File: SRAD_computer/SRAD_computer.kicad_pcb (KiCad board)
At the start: 2 copper layers, 49 parts, among them J1 USB_B_Micro, J2 Conn_01x02, U1 NCP1117-3.3_SOT223, U2 W25Q128JVS, U3 RP2040, U4 BME280, U5 MPU-9250, U6 SAM-M8Q-0-10, Y1 ABM8-272-T3

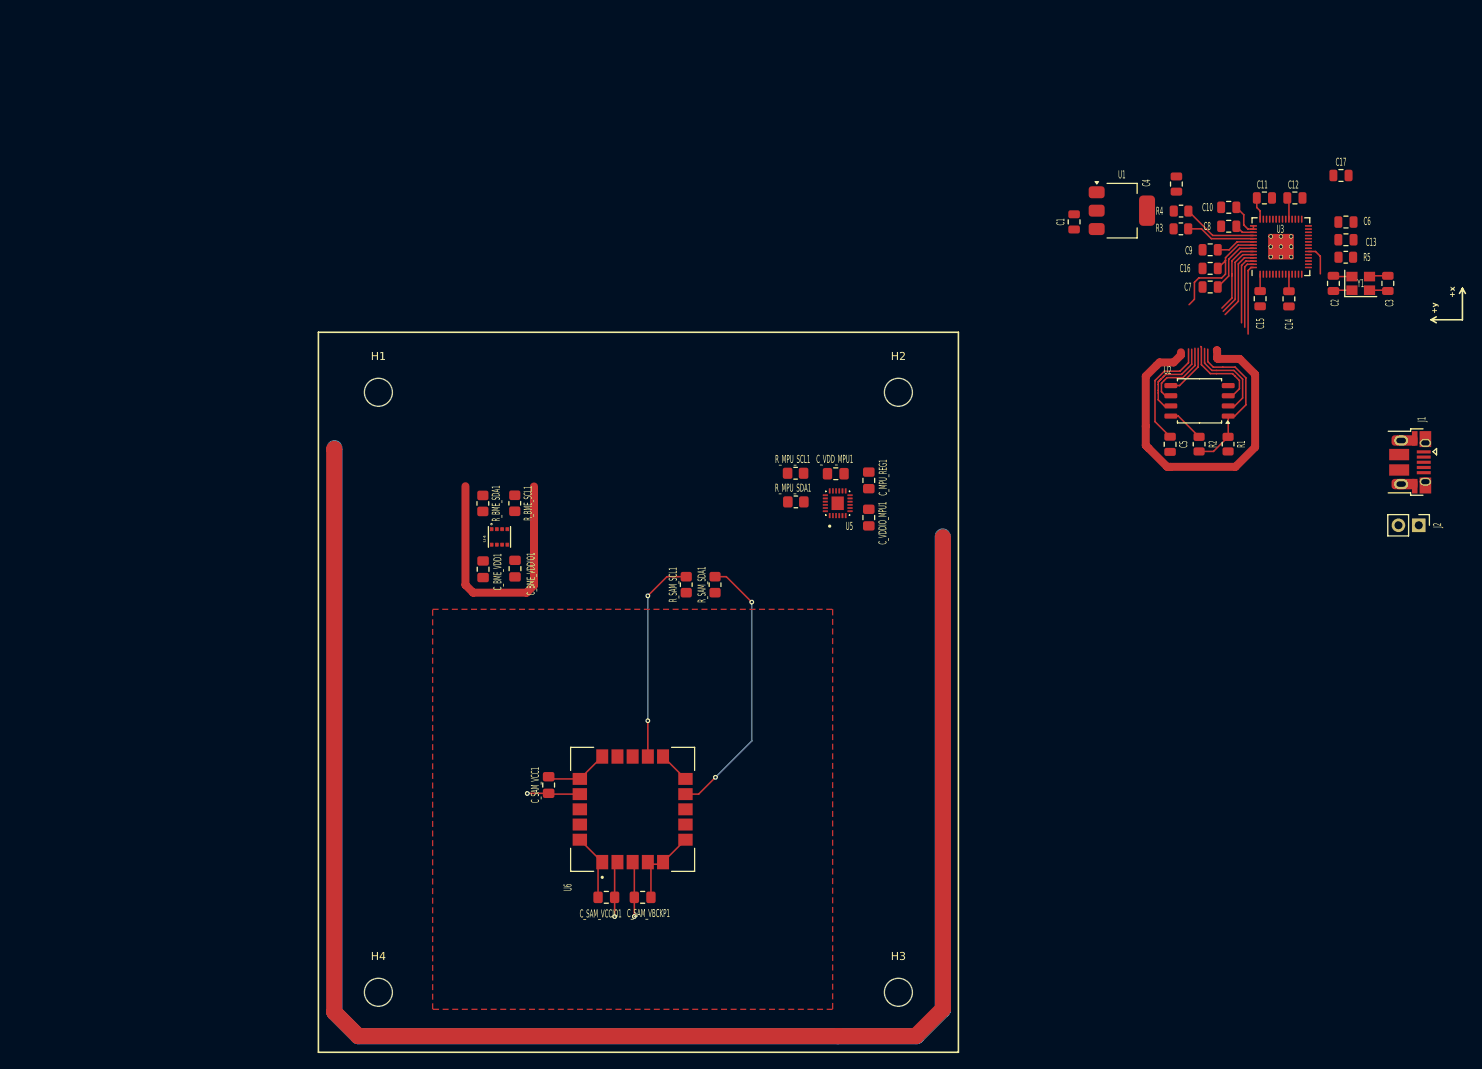
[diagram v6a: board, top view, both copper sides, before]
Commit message: Update PCB placement & 3D models added
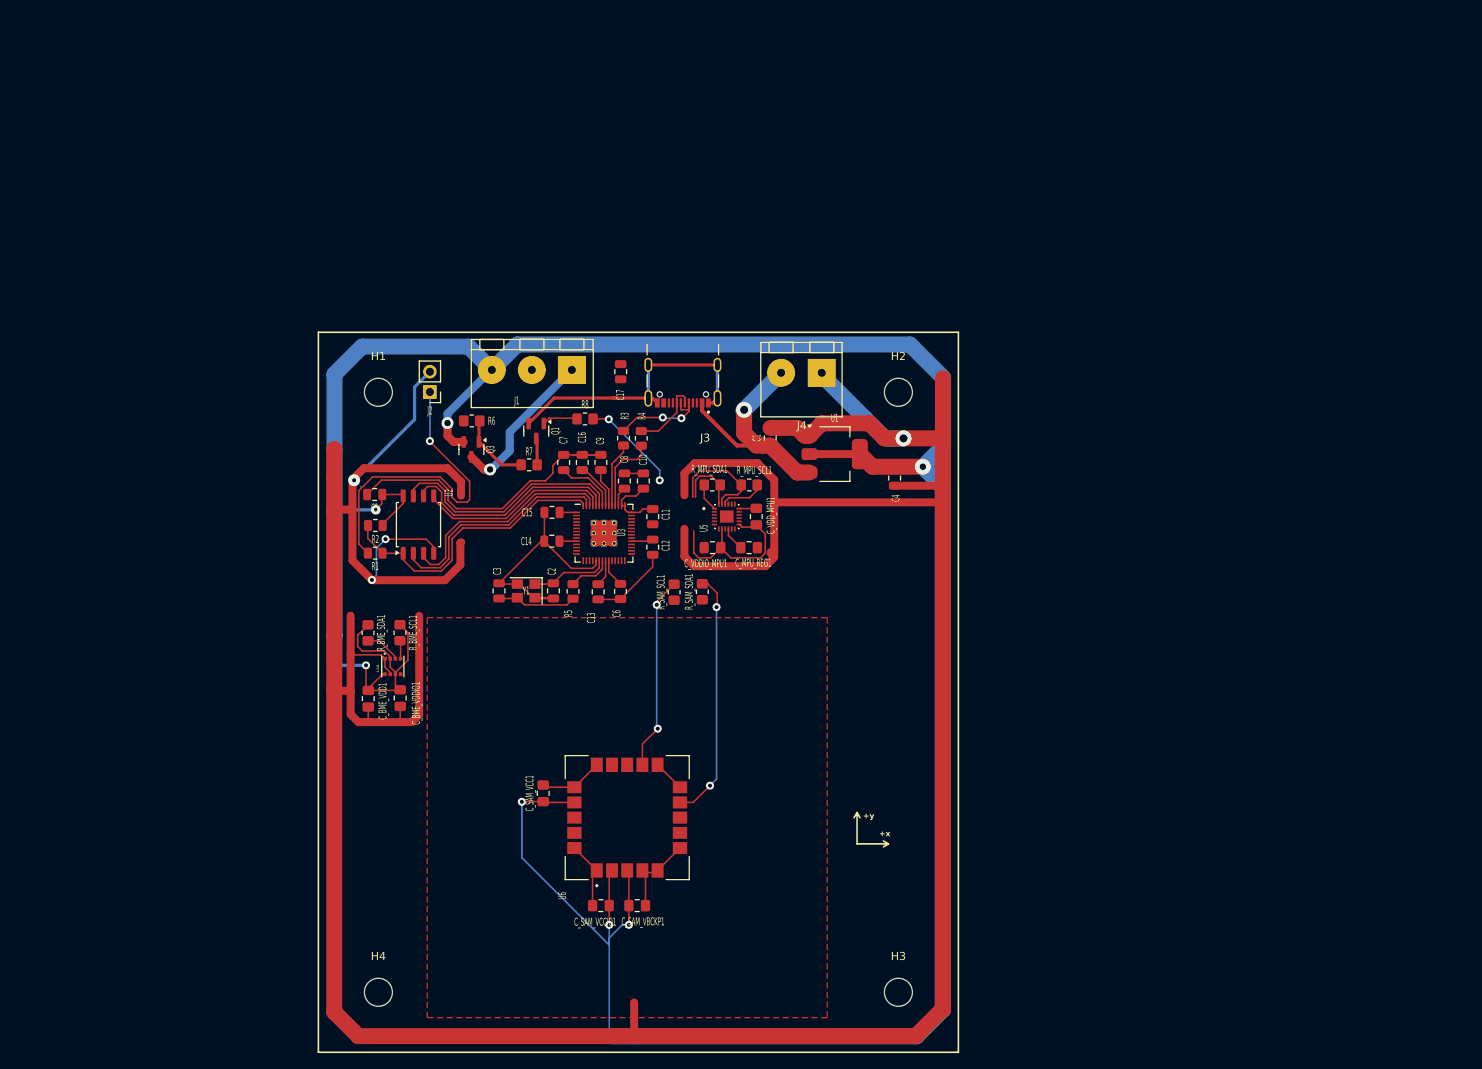
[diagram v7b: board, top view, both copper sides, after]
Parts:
- added J3: UJ20-C-H-G-SMT-1-P16-TR, my_lib:USB-C-samesky, F.Cu at (95.6, 51.5)
- added J4: Terminal_2, TCLib:Bornera_2_P5mm, F.Cu at (112.9, 55.1)
- added Q1: MMBT5551L, Package_TO_SOT_SMD:SOT-23, F.Cu at (77.2, 62.3)
- added Q3: FDN340P, Package_TO_SOT_SMD:SOT-23, F.Cu at (69.1, 64.6)
- added R6: R, TCLib:R_0805, F.Cu at (69.2, 61.1)
- added R7: R, TCLib:R_0805, F.Cu at (76.3, 66.6)
- added R8: R, TCLib:R_0805, F.Cu at (83.3, 60.8)
- J1: value USB_B_Micro -> Terminal_3; footprint RP2040_minimal_r2:USB_Micro-B_Amphenol_10103594-0001LF_Horizontal_modified -> TCLib:Bornera_3_P5mm
- moved J2 124.7 mm to (63.9, 57.5), turned to 180 degrees
- moved C3 117.6 mm to (72.6, 82.3), turned to 90 degrees
- moved Y1 111.2 mm to (76.0, 82.3), turned to 180 degrees
- moved R1 107.5 mm to (57.1, 77.6), turned to 180 degrees
- moved R5 105.2 mm to (81.8, 82.4), turned to -90 degrees
- moved C2 104.8 mm to (79.4, 82.3), turned to -90 degrees
- moved J1 104.3 mm to (81.7, 54.7), turned to 180 degrees
- moved R2 103.5 mm to (57.1, 74.2), turned to 180 degrees
- moved C13 103.3 mm to (85.0, 82.4), turned to -90 degrees
- moved C6 101.8 mm to (87.8, 82.4), turned to -90 degrees
- moved C5 99.6 mm to (57.0, 70.3), turned to 180 degrees
- moved U2 98.8 mm to (62.5, 74.0), turned to 90 degrees
- moved C14 97.0 mm to (79.2, 76.1), turned to 180 degrees
- moved C17 93.3 mm to (87.8, 54.9), turned to -90 degrees
- moved C15 92.5 mm to (79.2, 72.5), turned to 180 degrees
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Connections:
- C_SAM_VBCKP1 pad 2: Net-(U6-SDA) -> GND
- C_SAM_VCC1 pad 2: Net-(U6-SDA) -> GND
- C_SAM_VCCIO1 pad 2: Net-(U6-SDA) -> GND
- J1 pad 1: VBUS -> /V_cam
- J1 pad 2: /USB_D- -> GND
- J1 pad 3: /USB_D+ -> +3V3
- R_BME_SCL1 pad 2: /BME_SCL -> /SCL
- R_BME_SDA1 pad 2: /BME_SDA -> /SDA
- R_MPU_SCL1 pad 2: Net-(U5-SCL/SCLK) -> /SCL
- R_MPU_SDA1 pad 2: Net-(U5-SDA/SDI) -> /SDA
- R_SAM_SCL1 pad 2: Net-(U6-SCL) -> /SCL
- R_SAM_SDA1 pad 2: Net-(U6-SDA) -> /SDA
- U4 pad 3: /BME_SDA -> /SDA
- U4 pad 4: /BME_SCL -> /SCL
- U5 pad 23: Net-(U5-SCL/SCLK) -> /SCL
- U5 pad 24: Net-(U5-SDA/SDI) -> /SDA
- U6 pad 1: Net-(U6-SDA) -> GND
- U6 pad 10: Net-(U6-SDA) -> GND
- U6 pad 11: Net-(U6-SDA) -> GND
- U6 pad 12: Net-(U6-SCL) -> /SCL
- U6 pad 15: Net-(U6-SDA) -> GND
- U6 pad 16: Net-(U6-SDA) -> GND
- U6 pad 20: Net-(U6-SDA) -> GND
- U6 pad 4: Net-(U6-SDA) -> GND
- U6 pad 5: Net-(U6-SDA) -> GND
- U6 pad 6: Net-(U6-SDA) -> GND
- U6 pad 9: Net-(U6-SDA) -> /SDA
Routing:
- net +3V3: track 72.5 -> 462.4 mm, vias 3 -> 7
- net GND: track 293.1 -> 613.1 mm, vias 0 -> 4
- net (no net): track 208.4 -> 0.00 mm
- net Net-(U6-SDA): track 64.5 -> 0.00 mm, vias 2 -> 0
- net /SDA: track 0.00 -> 44.3 mm, vias 0 -> 2
- net /SCL: track 0.00 -> 40.4 mm, vias 0 -> 2
- net /~{USB_BOOT}: track 0.00 -> 40.4 mm, vias 0 -> 1
- net VBUS: track 0.00 -> 31.1 mm, vias 0 -> 1
- net Net-(U6-SCL): track 25.9 -> 0.00 mm, vias 2 -> 0
- net /V_cam: track 0.00 -> 19.7 mm, vias 0 -> 1
- net /USB_D+: track 0.00 -> 13.0 mm, vias 0 -> 2
- net /power_cam: track 0.00 -> 12.3 mm, vias 0 -> 2
- net /USB_D-: track 0.00 -> 9.23 mm
- net /QSPI_SD3: track 20.9 -> 30.1 mm
- net Net-(Q3-G): track 0.00 -> 9.12 mm
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- added copper zone on B.Cu, net GND

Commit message: PCB v1
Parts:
- moved C14 4.59 mm to (79.0, 80.7)
- moved C17 3.67 mm to (88.6, 58.5)
- moved C11 3.55 mm to (91.7, 76.6)
- moved C12 3.55 mm to (91.7, 80.4)
- moved C3 3.55 mm to (72.5, 85.9)
- moved C_BME_VDDIO1 3.55 mm to (60.1, 99.3)
- moved C_MPU_REG1 3.55 mm to (103.7, 80.5)
- moved R_MPU_SDA1 3.55 mm to (99.1, 72.6)
- moved C13 3.55 mm to (84.8, 86.0)
- moved C15 3.55 mm to (79.1, 76.1)
- moved C16 3.55 mm to (82.9, 69.8)
- moved C2 3.55 mm to (79.3, 85.9)
- moved C7 3.55 mm to (80.5, 69.8)
- moved C9 3.55 mm to (85.2, 69.8)
- moved C_BME_VDD1 3.55 mm to (56.1, 99.4)
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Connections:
- J1 pad 3: +3V3 -> VBUS
- Q3 pad 2: +3V3 -> VBUS
- R6 pad 1: +3V3 -> VBUS
- R8 pad 1: /power_cam -> /GPIO18
- R_BME_SCL1 pad 2: /SCL -> /GPIO17
- R_BME_SDA1 pad 2: /SDA -> /GPIO16
- R_MPU_SCL1 pad 2: /SCL -> /GPIO17
- R_MPU_SDA1 pad 2: /SDA -> /GPIO16
- R_SAM_SCL1 pad 2: /SCL -> /GPIO17
- R_SAM_SDA1 pad 2: /SDA -> /GPIO16
- U4 pad 3: /SDA -> /GPIO16
- U4 pad 4: /SCL -> /GPIO17
- U4 pad 5: unconnected-(U4-SDO-Pad5) -> GND
- U5 pad 23: /SCL -> /GPIO17
- U5 pad 24: /SDA -> /GPIO16
- U6 pad 12: /SCL -> /GPIO17
- U6 pad 9: /SDA -> /GPIO16
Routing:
- net /GPIO16: track 0.00 -> 108.2 mm, vias 0 -> 2
- net GND: track 613.1 -> 720.4 mm
- net /GPIO17: track 0.00 -> 103.2 mm, vias 0 -> 3
- net VBUS: track 31.1 -> 85.6 mm, vias 1 -> 2
- net /SDA: track 44.3 -> 0.00 mm, vias 2 -> 0
- net /SCL: track 40.4 -> 0.00 mm, vias 2 -> 0
- net /GPIO18: track 0.00 -> 27.6 mm, vias 0 -> 2
- net /power_cam: track 12.3 -> 0.00 mm, vias 2 -> 0
- net +3V3: track 462.4 -> 470.2 mm, vias 7 -> 11
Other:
- board text added: "Avionics&Recovery Hertter, Jose Ivan Diaz Guzmán, Ezequiel"
